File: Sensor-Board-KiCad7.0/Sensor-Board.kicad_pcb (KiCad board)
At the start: 2 copper layers, 75.4 x 75.4 mm, 128 parts, among them J1 B4B-XH-A, U1 OPA396DCKT, U10 BME680, U11 OPA396DCKT, U12 OPA396DCKT, U13 TCA9548AMRGER, U14 OPA396DCKT, U15 MMBFJ177LT1, U16 MMBFJ177LT1, U17 MMBFJ177LT1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

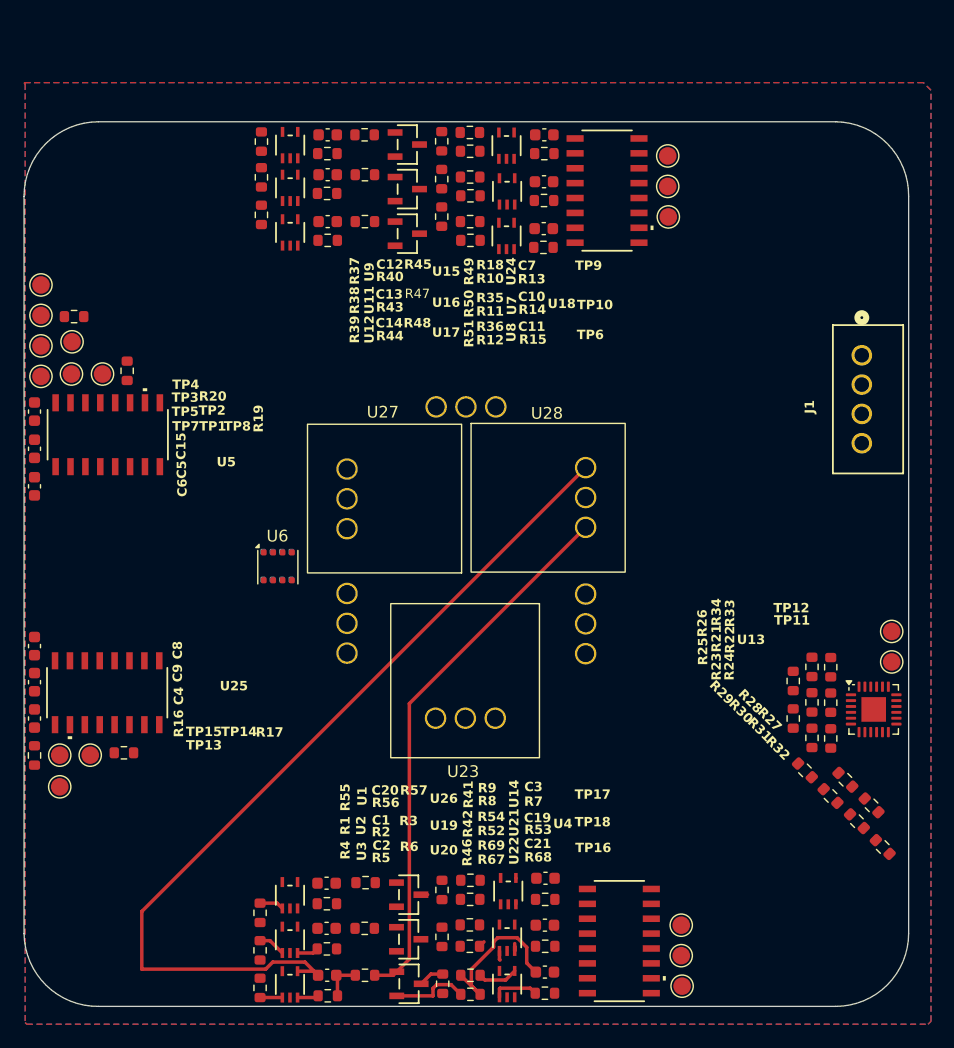
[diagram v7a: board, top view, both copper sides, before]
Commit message: Moved components around
Moved resistors and test points around. Continued trying to route vias along the board.
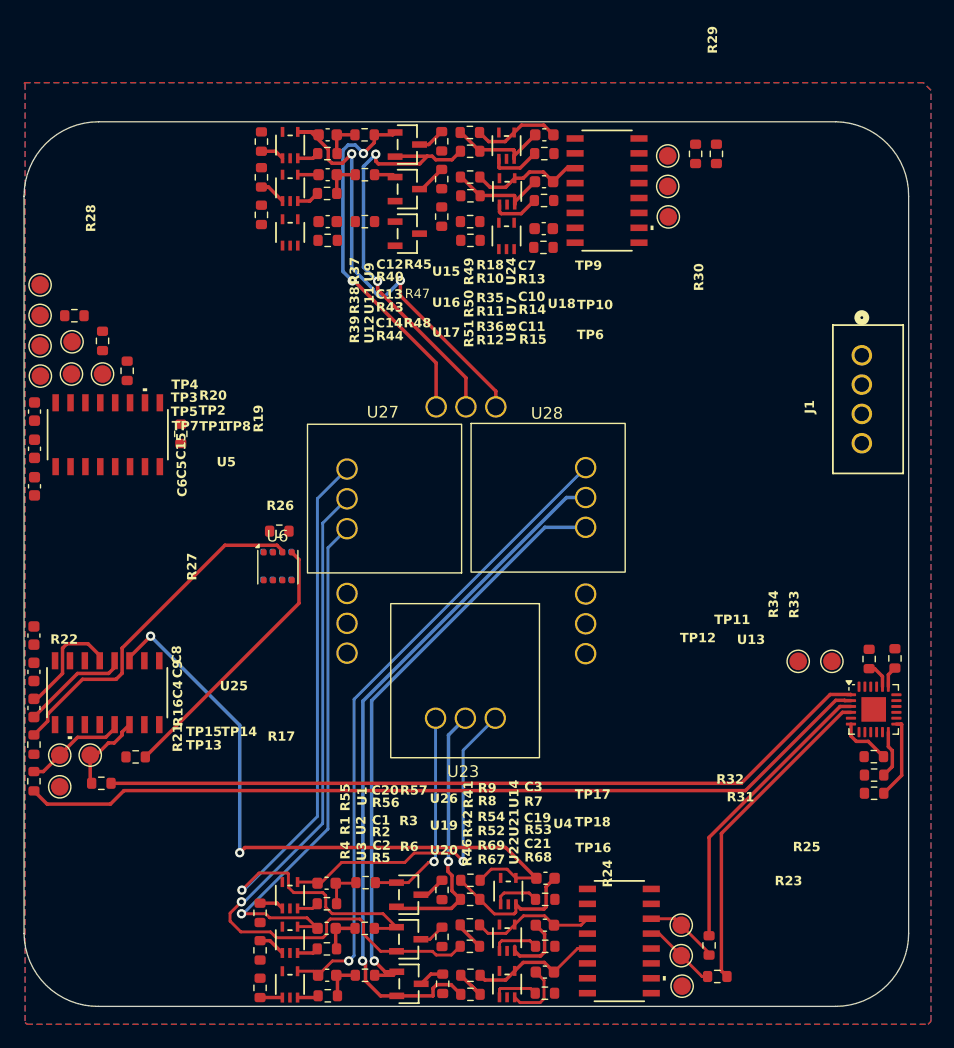
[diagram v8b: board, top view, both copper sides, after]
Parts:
- moved R28 73.6 mm to (106.7, 76.6), turned to 90 degrees
- moved R27 66.9 mm to (113.3, 84.5), turned to -90 degrees
- moved R21 66.7 mm to (100.8, 114.1), turned to -90 degrees
- moved R22 62.6 mm to (106.5, 114.3), turned to 0 degrees
- moved R30 56.0 mm to (157.2, 60.6), turned to -90 degrees
- moved R29 53.1 mm to (159.0, 60.6), turned to -90 degrees
- moved R26 45.6 mm to (121.7, 92.8), turned to 0 degrees
- moved R23 21.9 mm to (159.1, 130.8), turned to 0 degrees
- moved R24 20.5 mm to (158.4, 128.1)
- moved TP12 8.37 mm to (166.0, 103.9)
- moved R25 7.60 mm to (172.4, 112.0), turned to 0 degrees
- moved R32 6.18 mm to (172.4, 113.6), turned to 0 degrees
- moved R33 5.53 mm to (174.2, 103.7)
- moved TP11 5.10 mm to (168.8, 103.9)
- moved R34 4.92 mm to (172.0, 103.7)
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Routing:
- net Net-(U13-SC0): track 0.00 -> 73.8 mm
- net Net-(U13-SD0): track 0.00 -> 66.2 mm
- net Sens1_CO: track 0.00 -> 63.9 mm, vias 0 -> 1
- net Ref1_CO: track 0.14 -> 58.8 mm, vias 0 -> 1
- net AOut1_NO2: track 0.04 -> 56.7 mm, vias 0 -> 2
- net Sens1_SO2: track 6.57 -> 60.1 mm, vias 0 -> 1
- net Count1_CO: track 0.21 -> 45.4 mm, vias 0 -> 1
- net Count2_NO2: track 0.00 -> 38.1 mm, vias 0 -> 2
- net Sens2_NO2: track 0.00 -> 37.0 mm, vias 0 -> 2
- net Ref2_NO2: track 0.00 -> 31.4 mm, vias 0 -> 2
- net 680_SDA2: track 0.00 -> 29.8 mm
- net Count1_NO2: track 0.14 -> 28.8 mm, vias 0 -> 1
- net Net-(U13-SC1): track 0.00 -> 27.7 mm
- net Net-(U13-SD1): track 0.00 -> 25.1 mm
- net 680_SCL2: track 0.00 -> 23.1 mm
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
